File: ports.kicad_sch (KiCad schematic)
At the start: 6 parts, among them J1 PCA9865 2, J12 I2C, J2 I2S, J4 IMU, J6 Expansion

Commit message: Cleaned revision 2.
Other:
- moved on the sheet: JP5

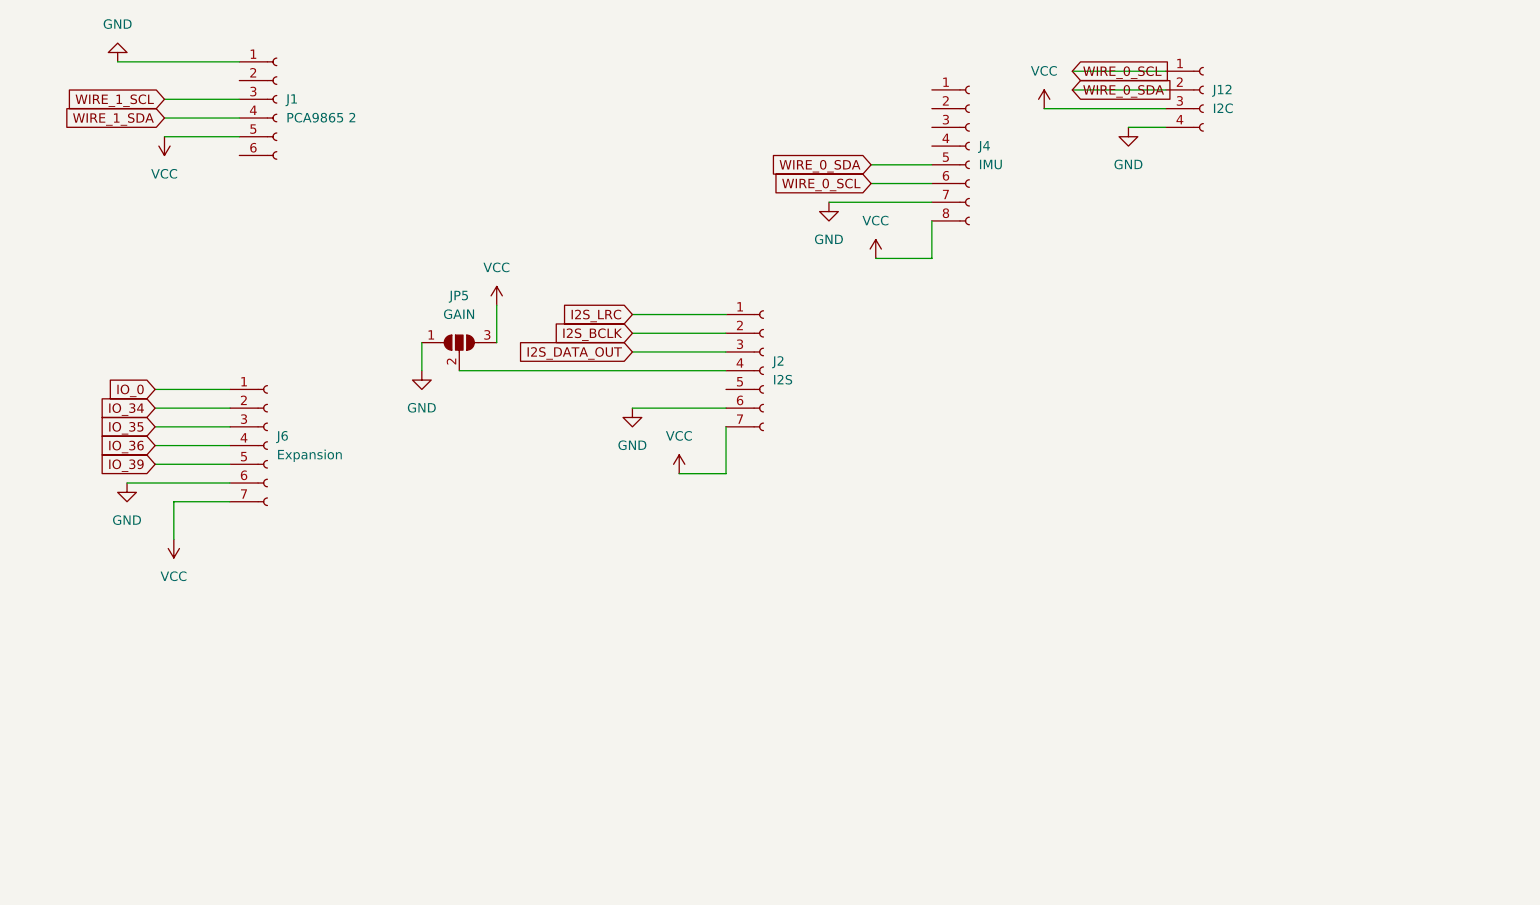
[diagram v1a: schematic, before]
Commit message: Very minor tweaks for board version 3.
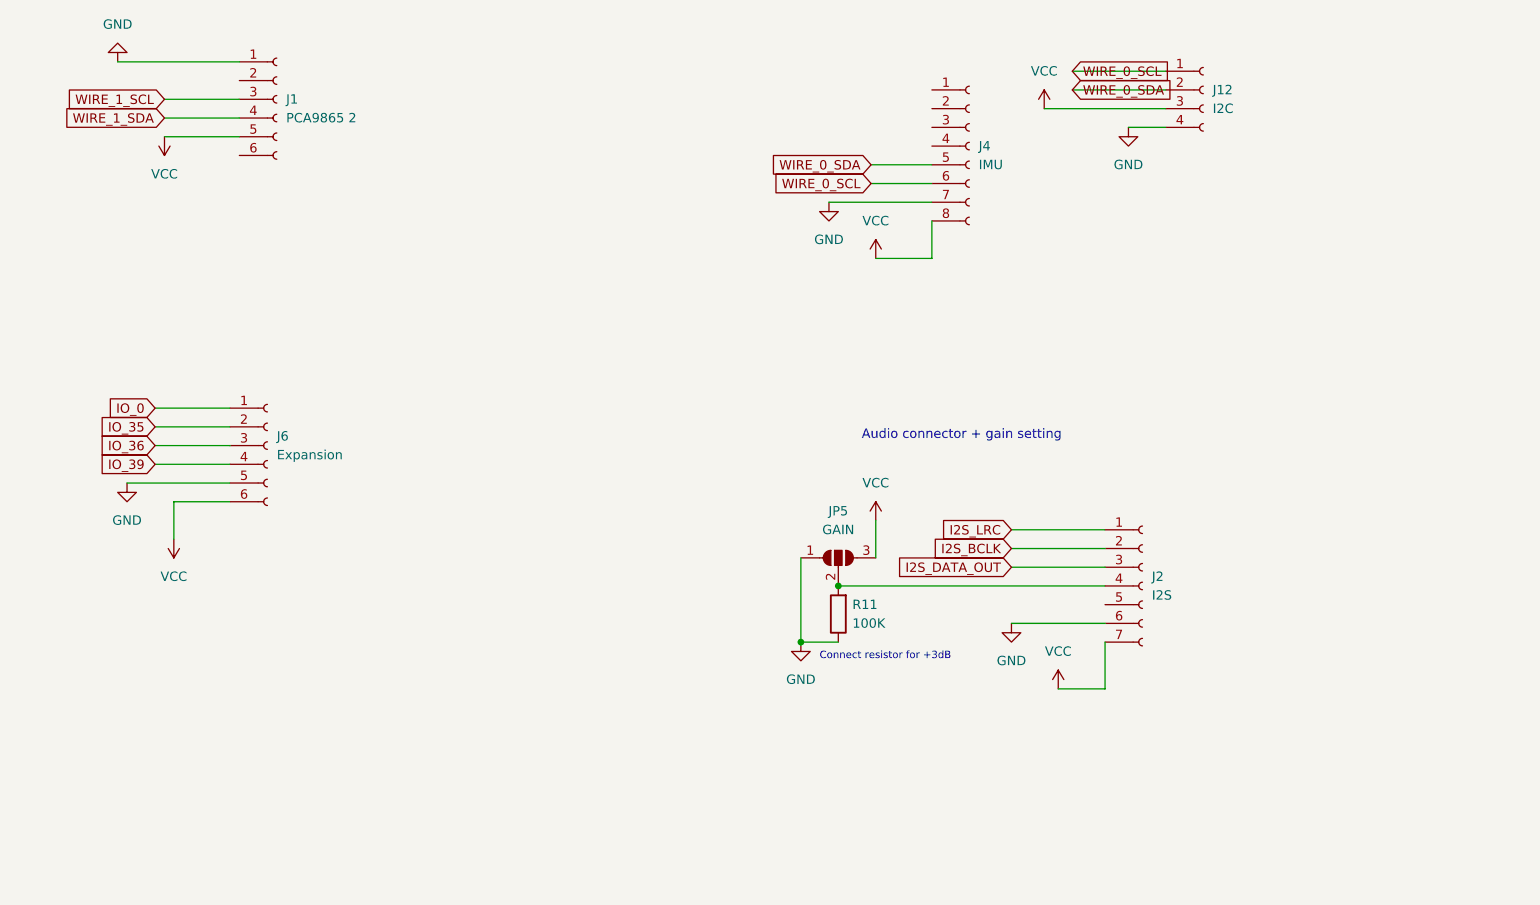
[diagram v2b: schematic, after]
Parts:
- added R11: 100K, Resistor_SMD:R_1206_3216Metric_Pad1.30x1.75mm_HandSolder, symbol Device:R
- J6: symbol Connector:Conn_01x07_Female -> Connector:Conn_01x06_Female
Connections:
- net IO_34 is gone; now on net IO_35: J6.2 (Pin_2)
- net GND: now also J6.5 (Pin_5), R11.1; no longer J6.6 (Pin_6)
- net IO_35: no longer J6.3 (Pin_3)
- net IO_36: now also J6.3 (Pin_3); no longer J6.4 (Pin_4)
- net IO_39: now also J6.4 (Pin_4); no longer J6.5 (Pin_5)
- net VCC: now also J6.6 (Pin_6); no longer J6.7 (Pin_7)
- net at J2.4 (Pin_4), JP5.2 (C): now also R11.2
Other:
- note added: "Audio connector + gain setting"
- note added: "Connect resistor for +3dB"
- moved on the sheet: J2, JP5

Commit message: Upgrade to version 7, started adding new WROOM-S3
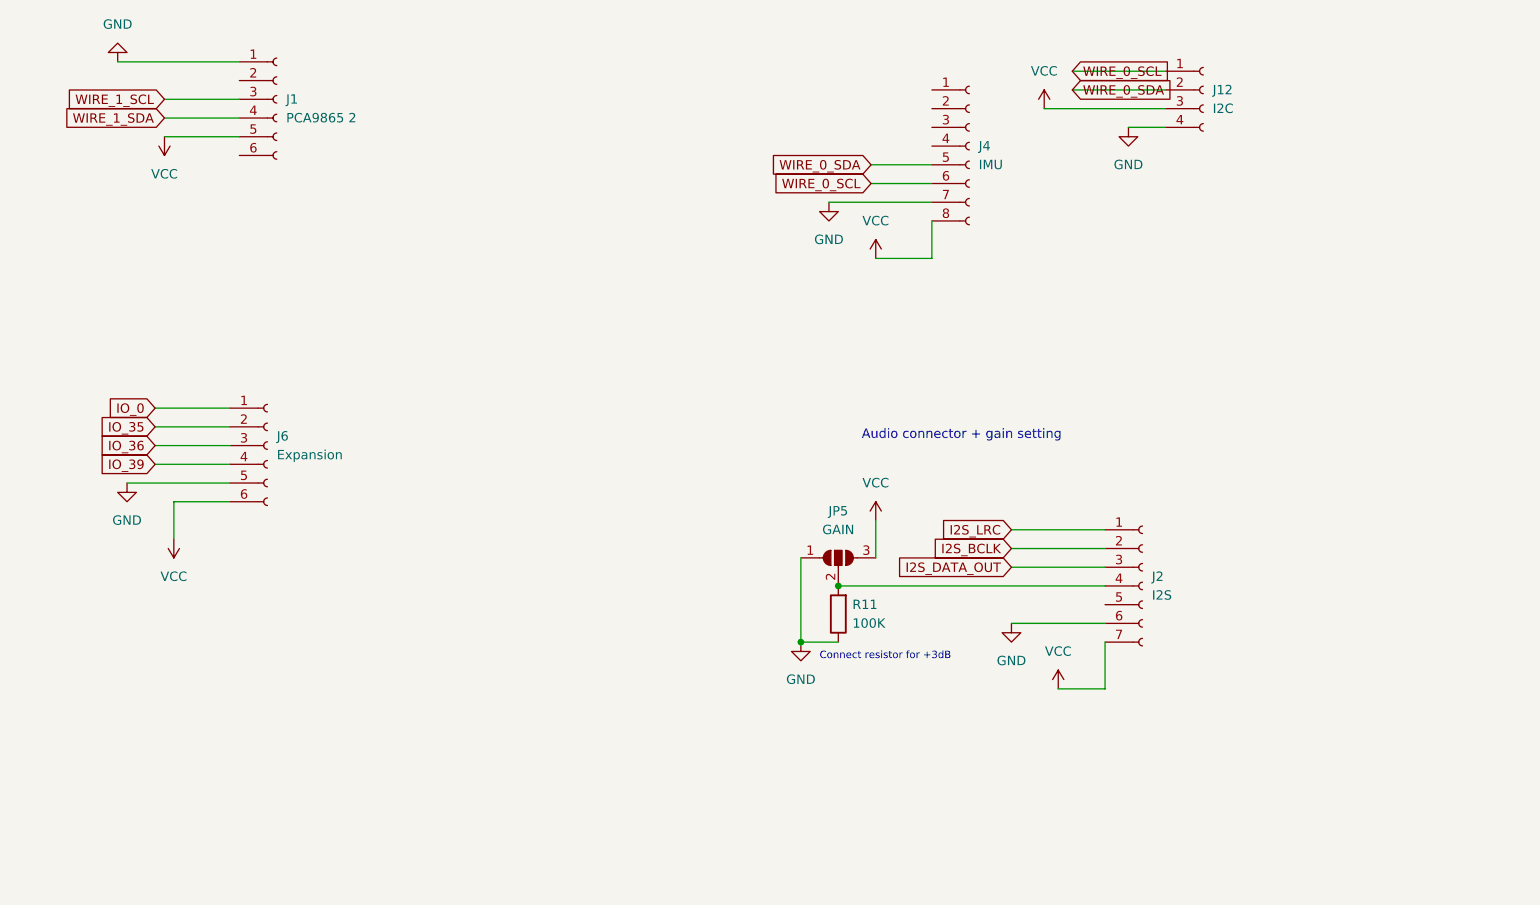
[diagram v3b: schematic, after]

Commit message: Removed old ESP32, added ESP32 S3.
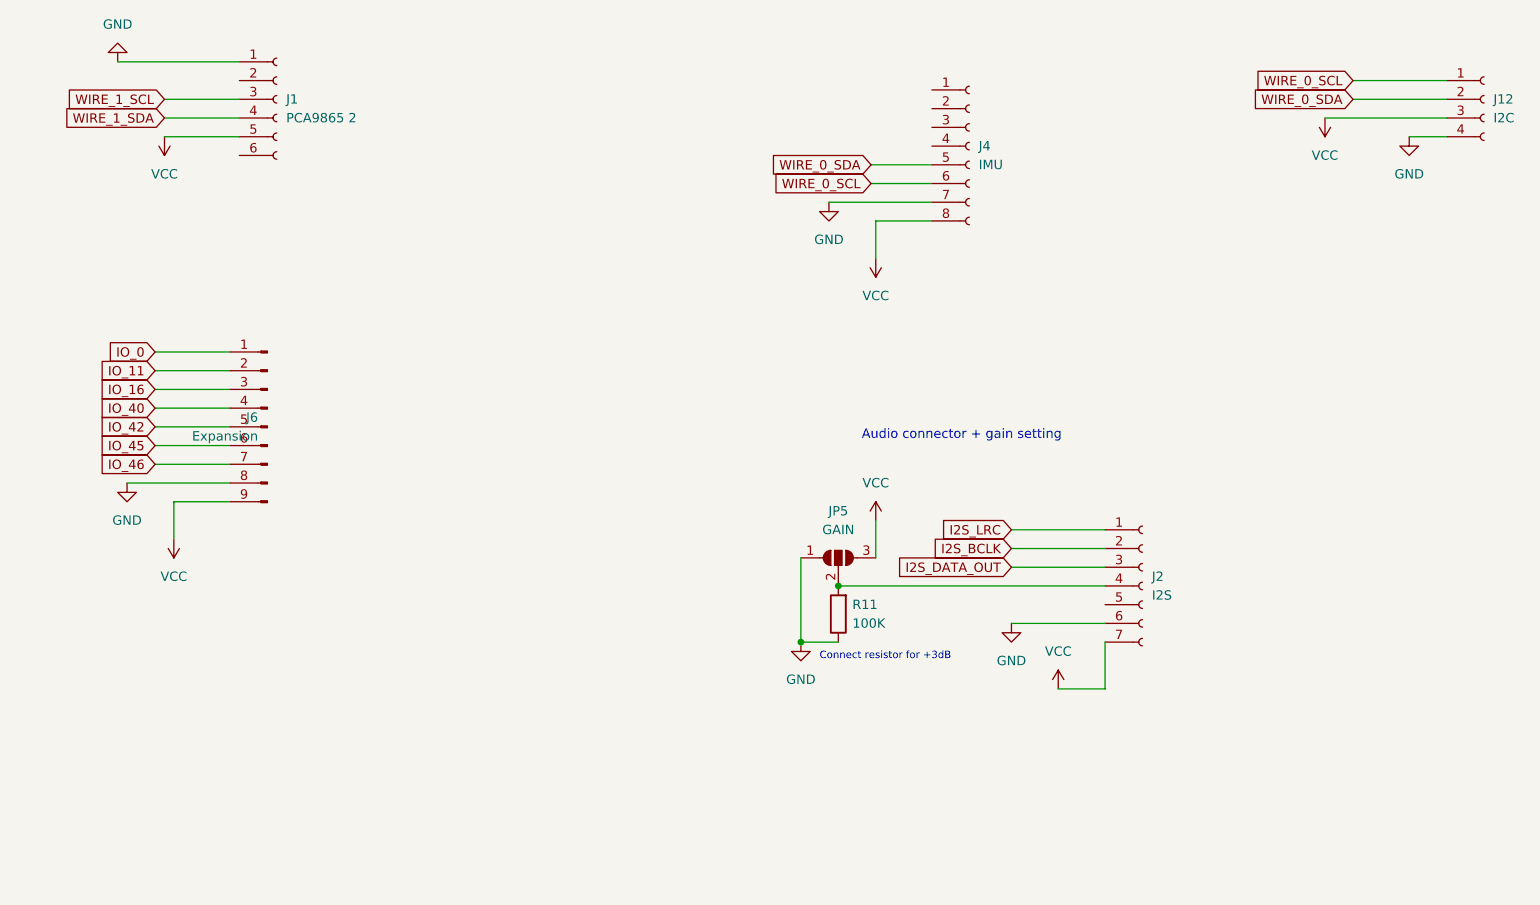
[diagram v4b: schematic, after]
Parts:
- J6: footprint Connector_PinSocket_2.54mm:PinSocket_1x07_P2.54mm_Vertical -> Connector_PinSocket_2.54mm:PinSocket_1x09_P2.54mm_Vertical; symbol Connector:Conn_01x06_Female -> Connector:Conn_01x09_Pin
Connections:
- net GND: now also J6.8 (Pin_8); no longer J6.5 (Pin_5)
- net VCC: now also J6.9 (Pin_9); no longer J6.6 (Pin_6)
- net IO_35 renamed IO_11
- net IO_36 renamed IO_16
- net IO_39 renamed IO_40
- new net IO_42: J6.5 (Pin_5)
- new net IO_45: J6.6 (Pin_6)
- new net IO_46: J6.7 (Pin_7)
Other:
- moved on the sheet: J12

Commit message: Finished routing board revision 3: ready for first PCB run.
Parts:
- added J15: USB_B_Micro, Connector_USB:USB_Micro-B_Amphenol_10104110_Horizontal, symbol Connector:USB_B_Micro
- J6: footprint Connector_PinSocket_2.54mm:PinSocket_1x09_P2.54mm_Vertical -> Connector_PinSocket_2.54mm:PinSocket_2x04_P2.54mm_Vertical; symbol Connector:Conn_01x09_Pin -> Connector_Generic:Conn_02x04_Odd_Even
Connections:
- net IO_0 is gone; now on net AUDIO GAIN: J6.1 (Pin_1)
- net IO_11 is gone; now on net IO_16: J6.2 (Pin_2)
- net GND: now also J6.7 (Pin_7), J15.5 (GND); no longer J6.8 (Pin_8)
- net IO_16: no longer J6.3 (Pin_3)
- net IO_40: now also J6.3 (Pin_3); no longer J6.4 (Pin_4)
- net IO_42: now also J6.4 (Pin_4); no longer J6.5 (Pin_5)
- net IO_45: now also J6.5 (Pin_5); no longer J6.6 (Pin_6)
- net IO_46: now also J6.6 (Pin_6); no longer J6.7 (Pin_7)
- net VCC: now also J6.8 (Pin_8); no longer J6.9 (Pin_9)
- net AUDIO GAIN: now reaches J2.4 (Pin_4), JP5.2 (C), R11.2
- new net USB_D+: J15.3 (D+)
- new net USB_D-: J15.2 (D-)

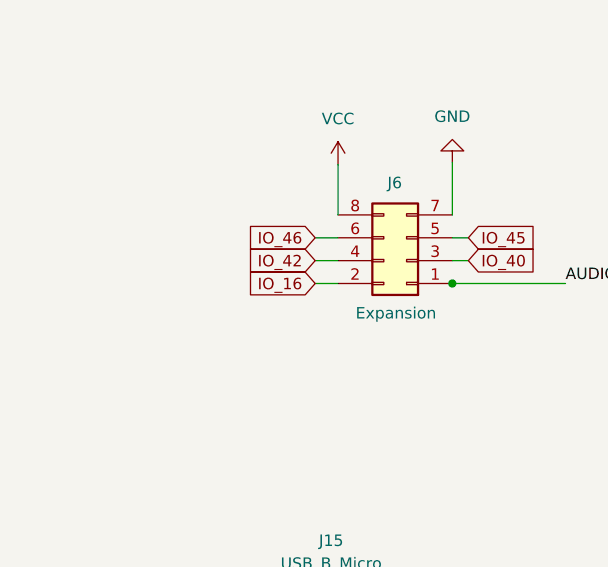
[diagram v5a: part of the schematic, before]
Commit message: Switched out GPIO3 for GPIO16 because it is a strapping pin with no pullup.
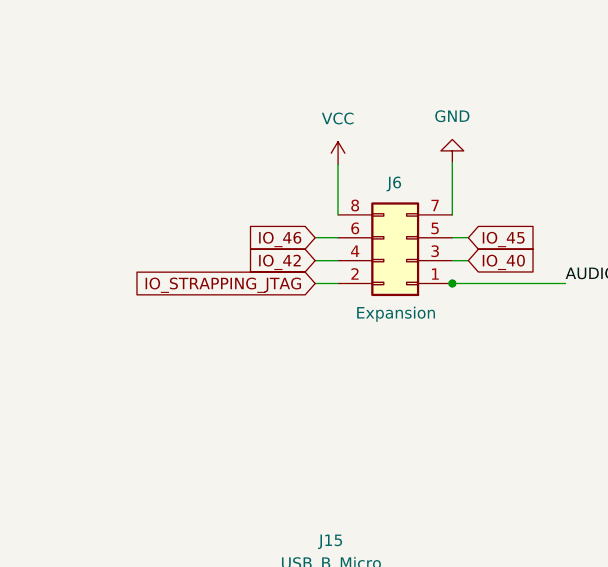
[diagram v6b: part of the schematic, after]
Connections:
- net IO_16 renamed IO_STRAPPING_JTAG
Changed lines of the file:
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@@
     )
   )
-  (global_label "IO_16" (shape input) (at 57.277 83.185 180) (fields_autoplaced)
+  (global_label "IO_STRAPPING_JTAG" (shape input) (at 57.277 83.185 180) (fields_autoplaced)
     (effects (font (size 1.27 1.27)) (justify right))
-    (property "Intersheetrefs" "${INTERSHEET_REFS}" (at 49.0493 83.185 0)
+    (property "Intersheetrefs" "${INTERSHEET_REFS}" (at 35.9259 83.185 0)
       (effects (font (size 1.27 1.27)) (justify right) hide)
     )
